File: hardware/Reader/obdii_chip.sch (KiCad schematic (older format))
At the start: 20 parts, among them IC2 STN2120, X1 ECS-2033-160-AU (16MHz)

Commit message: Completed Reader schematics for version 0.0.01
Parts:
- removed JP_STN_1: \"HW Reset\", symbol Device:Jumper
- added J_STN_1, J_STN_3, J_STN_RST1: 282832-2, footprints:282832-2, symbol 2828322:282832-2
- added SW_STN_1: PTS647SK38SMTR2LFS, footprints:PTS647SK38SMTR2LFS, symbol PTS647SK38SMTR2LFS:PTS647SK38SMTR2LFS
- IC2: footprint (none) -> Package_DFN_QFN:QFN-44-1EP_8x8mm_P0.65mm_EP6.45x6.45mm_ThermalVias
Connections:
- wire segments 152 -> 169
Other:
- moved on the sheet: C_STN_2, LED_STN_1, LED_STN_2, LED_STN_3, R_STN_2, R_STN_3, R_STN_4, R_STN_5, R_STN_6, R_STN_7

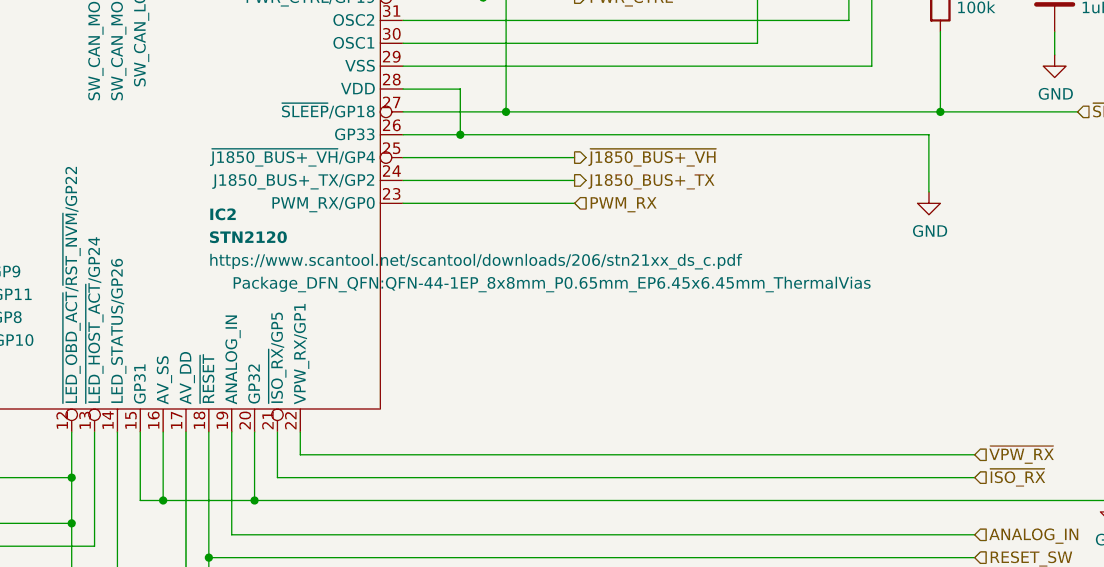
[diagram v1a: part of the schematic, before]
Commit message: Minor changes to schematic design for clarity. Added important IC datasheets. Exported schematics and rough gerber files
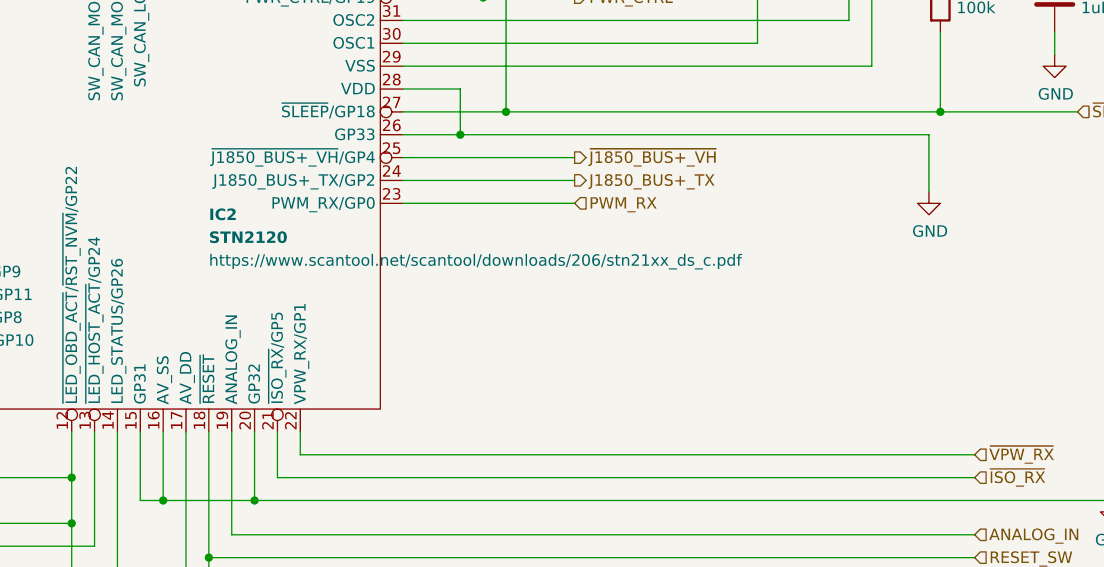
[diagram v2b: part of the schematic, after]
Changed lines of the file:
@@
 F 0 "IC2" H 6250 3050 50  0000 L CNB
 F 1 "STN2120" H 6250 2950 50  0000 L CNB
-F 2 "Package_DFN_QFN:QFN-44-1EP_8x8mm_P0.65mm_EP6.45x6.45mm_ThermalVias" H 7750 2750 50  0000 C CNN
+F 2 "Package_DFN_QFN:QFN-44-1EP_8x8mm_P0.65mm_EP6.45x6.45mm_ThermalVias" H 7750 2750 50  0001 C CNN
 F 3 "https://www.scantool.net/scantool/downloads/206/stn21xx_ds_c.pdf" H 6250 2850 50  0000 L CNN
 	1    6050 3350

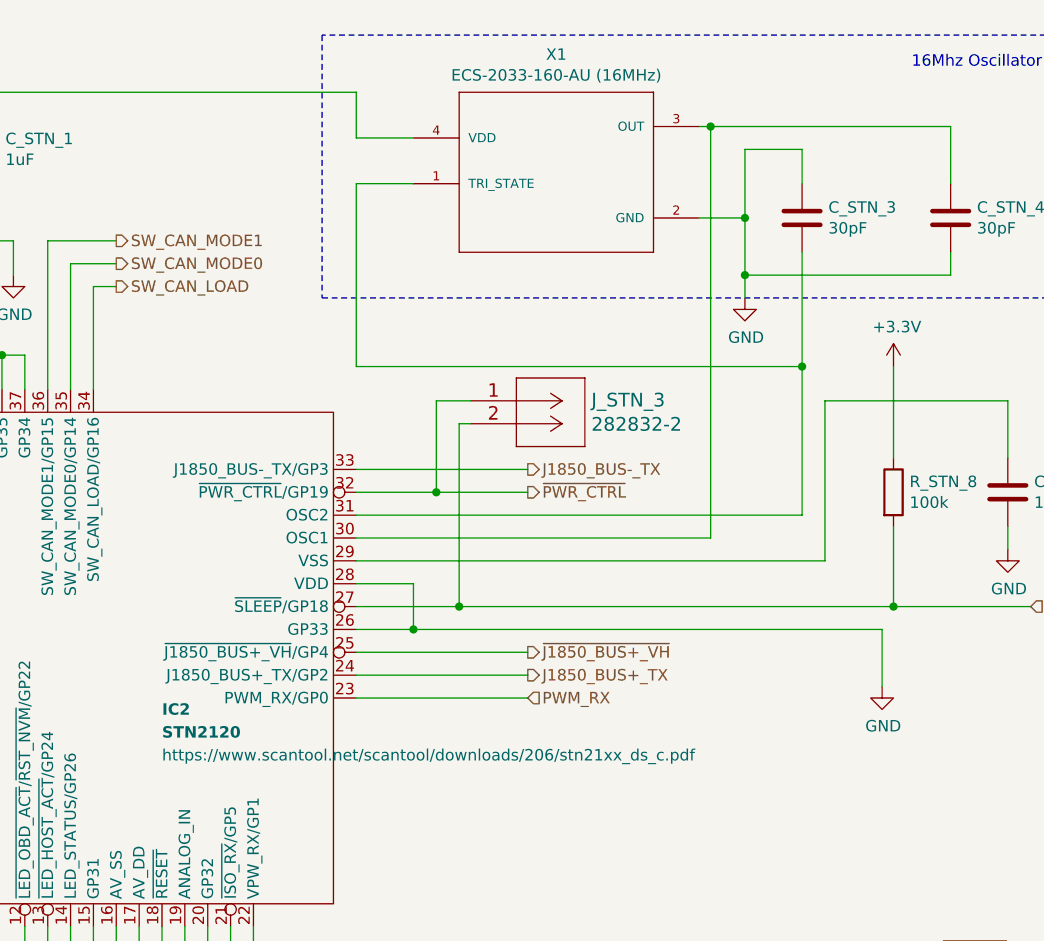
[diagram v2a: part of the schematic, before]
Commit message: Added ESD Protection. Fixed minor bugs on schematic. Attempted placement of components
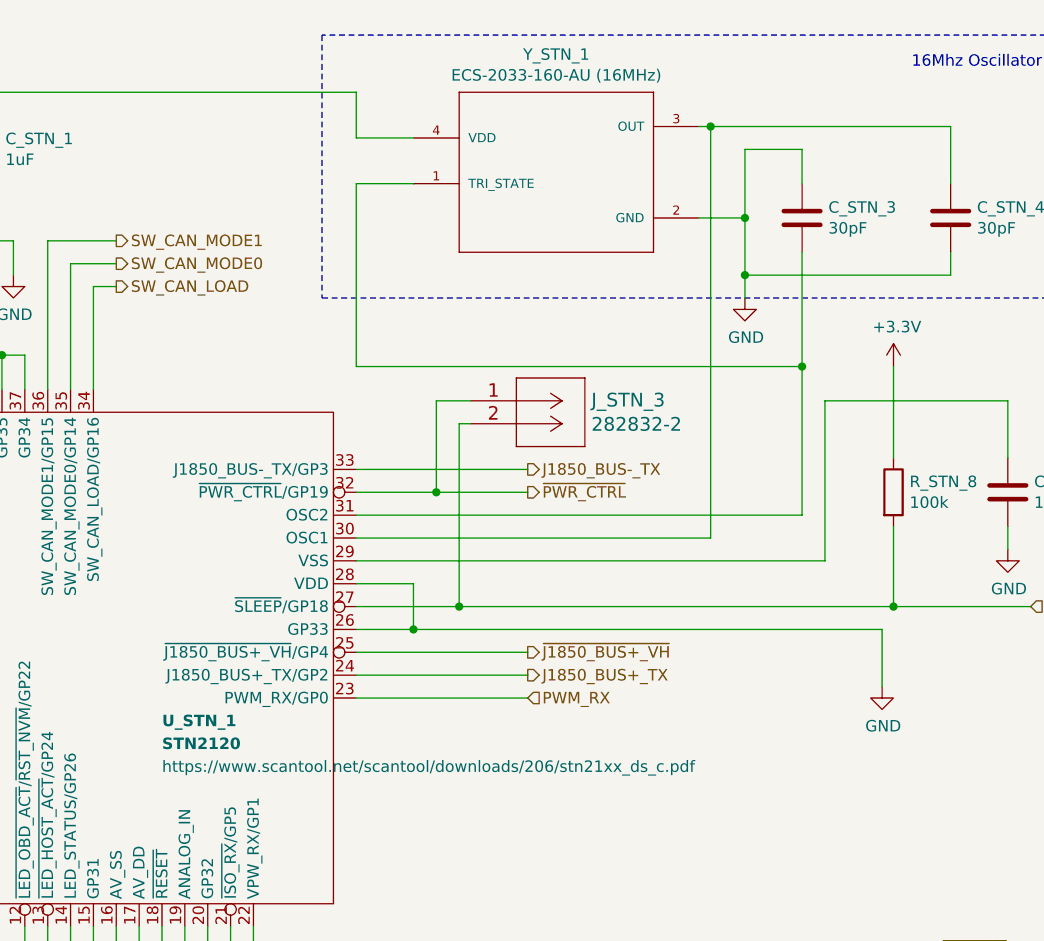
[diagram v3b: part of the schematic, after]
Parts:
- renumbered IC2 to U_STN_1, X1 to Y_STN_1
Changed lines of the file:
@@
 $Descr USLetter 11000 8500
 encoding utf-8
-Sheet 15 18
+Sheet 10 19
 Title "CANnect Reader | OBDII Chip (STN2110)"
-Date "2020-10-20"
-Rev "0.0.01"
+Date "2020-10-25"
+Rev "0.0.03"
 Comp "CANtech"
 Comment1 "Created by Choong Jin Ng | jin8383@gmail.com"
@@
 P 6050 3350
 AR Path="/5F95F80B/5FC0708B" Ref="U?"  Part="1"
-AR Path="/5F95F80B/5FC0631B/5FC0708B" Ref="IC2"  Part="1"
-F 0 "IC2" H 6250 3050 50  0000 L CNB
-F 1 "STN2120" H 6250 2950 50  0000 L CNB
+AR Path="/5F95F80B/5FC0631B/5FC0708B" Ref="U_STN_1"  Part="1"
+F 0 "U_STN_1" H 6250 3000 50  0000 L CNB
+F 1 "STN2120" H 6250 2900 50  0000 L CNB
 F 2 "Package_DFN_QFN:QFN-44-1EP_8x8mm_P0.65mm_EP6.45x6.45mm_ThermalVias" H 7750 2750 50  0001 C CNN
-F 3 "https://www.scantool.net/scantool/downloads/206/stn21xx_ds_c.pdf" H 6250 2850 50  0000 L CNN
+F 3 "https://www.scantool.net/scantool/downloads/206/stn21xx_ds_c.pdf" H 6250 2800 50  0000 L CNN
 	1    6050 3350
 	1    0    0    -1
@@
 	7350 3300 9400 3300
 $Comp
-L ECS-2033-160-AU:ECS-2033-160-AU X1
+L ECS-2033-160-AU:ECS-2033-160-AU Y_STN_1
 U 1 1 5FDAE336
 P 8000 1250
-F 0 "X1" H 7975 1715 50  0000 C CNN
+F 0 "Y_STN_1" H 7975 1715 50  0000 C CNN
 F 1 "ECS-2033-160-AU (16MHz)" H 7975 1624 50  0000 C CNN
 F 2 "footprints:OSC_ECS-2033-160-AU" H 8000 1250 50  0001 L BNN
@@
 	0    1    1    0
 $EndComp
-$Comp
-L PTS647SK38SMTR2LFS:PTS647SK38SMTR2LFS SW_STN_1
-U 1 1 5F93A6E5
-P 4250 5700
-F 0 "SW_STN_1" H 5050 6087 60  0000 C CNN
-F 1 "PTS647SK38SMTR2LFS" H 5050 5981 60  0000 C CNN
-F 2 "footprints:PTS647SK38SMTR2LFS" H 5050 5940 60  0001 C CNN
-F 3 "https://www.ckswitches.com/media/2567/pts647.pdf" H 4250 5700 60  0001 C CNN
-	1    4250 5700
-	1    0    0    -1
-$EndComp
 Connection ~ 6250 5150
 Wire Wire Line
@@
 Wire Wire Line
 	4400 6200 4400 6550
+$Comp
+L PTS647SK38SMTR2LFS:PTS647SK38SMTR2LFS SW_STN_1
+U 1 1 5F93A6E5
+P 4250 5700
+F 0 "SW_STN_1" H 5050 6087 60  0000 C CNN
+F 1 "PTS647SK38SMTR2LFS" H 5050 5981 60  0000 C CNN
+F 2 "footprints:PTS647SK38SMTR2LFS" H 5050 5940 60  0001 C CNN
+F 3 "https://www.ckswitches.com/media/2567/pts647.pdf" H 4250 5700 60  0001 C CNN
+	1    4250 5700
+	1    0    0    -1
+$EndComp
 $EndSCHEMATC

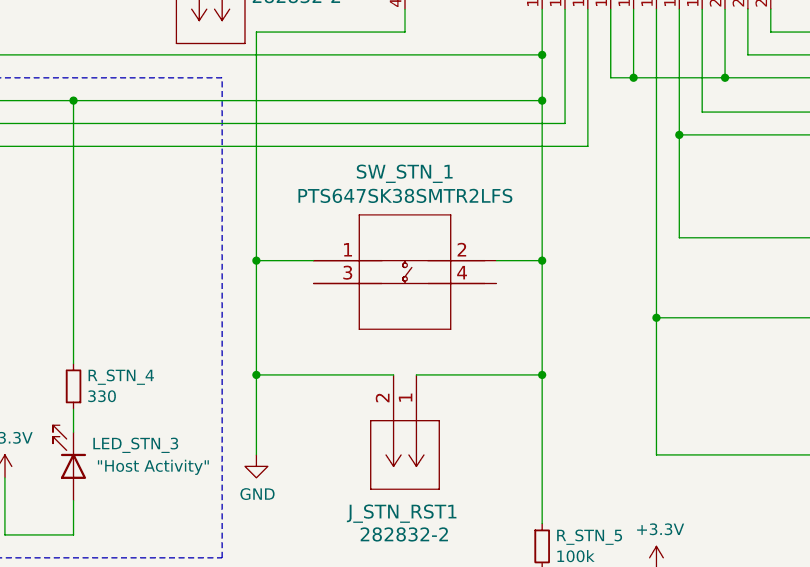
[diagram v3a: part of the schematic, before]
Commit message: Fixed bugs on the reader schematic. Exported Schematic Electrical report
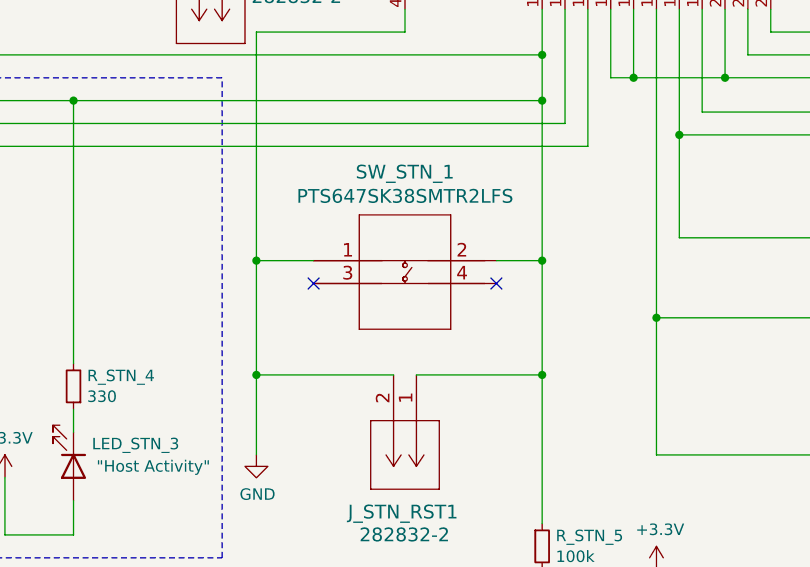
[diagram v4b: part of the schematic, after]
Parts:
- CP_STN_1: Manufacturer (none) -> Panasonic Electronic Components; Part Name (none) -> EEEFP1E100AR; Vendor (none) -> DigiKey Canada; digikeypn (none) -> PCE4539CT-ND
- C_STN_1, C_STN_2, C_STN_5: Manufacturer (none) -> Kermet; Part Name (none) -> C0603C105K4RACTU; Vendor (none) -> DigiKey Canada; digikeypn (none) -> 399-7847-1-ND
- C_STN_3, C_STN_4: footprint footprints:CAPC2012X88N -> footprints:CAPC1608X90N; Manufacturer (none) -> Kermet; Part Name (none) -> C0603C300J5GACTU; Vendor (none) -> DigiKey Canada; digikeypn (none) -> 399-9057-1-ND
- J_STN_1, J_STN_3, J_STN_RST1: Manufacturer (none) -> TE Connectivity AMP Connectors; Vendor (none) -> DigiKey Canada; digikeypn (none) -> A113314-ND
- LED_STN_1: Manufacturer (none) -> Würth Elektronik; Vendor (none) -> DigiKey Canada; digikeypn (none) -> 732-4978-1-ND
- LED_STN_2: Manufacturer (none) -> Würth Elektronik; Vendor (none) -> DigiKey Canada; digikeypn (none) -> 732-4981-1-ND
- LED_STN_3: Manufacturer (none) -> Würth Elektronik; Vendor (none) -> DigiKey Canada; digikeypn (none) -> 732-4980-1-ND
- R_STN_1: Manufacturer (none) -> Samsung Electro-Mechanics; Vendor (none) -> DigiKey Canada; digikeypn (none) -> 1276-3484-1-ND
- R_STN_2, R_STN_3, R_STN_4: Manufacturer (none) -> Panasonic Electronic Components; Vendor (none) -> DigiKey Canada; digikeypn (none) -> P330FCT-ND
- R_STN_5, R_STN_8: Manufacturer (none) -> Yageo; Vendor (none) -> DigiKey Canada; digikeypn (none) -> 311-2395-1-ND
- R_STN_6: Manufacturer (none) -> Yageo; Vendor (none) -> DigiKey Canada; digikeypn (none) -> YAG2321CT-ND
- R_STN_7: Manufacturer (none) -> Bourns Inc.; Part Name (none) -> CR0402-FX-10R0GLF; Vendor (none) -> DigiKey Canada; digikeypn (none) -> CR0402-FX-10R0GLFCT-ND
- SW_STN_1: Manufacturer (none) -> C&K; Part Name (none) -> PTS647SK38SMTR2LFS; Vendor (none) -> DigiKey Canada; digikeypn (none) -> PTS647SK38SMTR2LFSCT-ND
- U_STN_1: Manufacturer (none) -> OBD Solutions; Part Name (none) -> STN2120; Vendor (none) -> ScanTool
- Y_STN_1: Manufacturer (none) -> ECS Inc.; Part Name (none) -> ECS-2033-160-AU (16MHz); Vendor (none) -> DigiKey Canada; digikeypn (none) -> XC1858CT-ND
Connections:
- no-connect marks 0 -> 2
